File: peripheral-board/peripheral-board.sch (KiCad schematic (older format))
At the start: 4 parts, among them CON1001 AVR-ISP-10, IC1001 ATTINY48-A, P1001 Peripheral Bus, P1002 Power

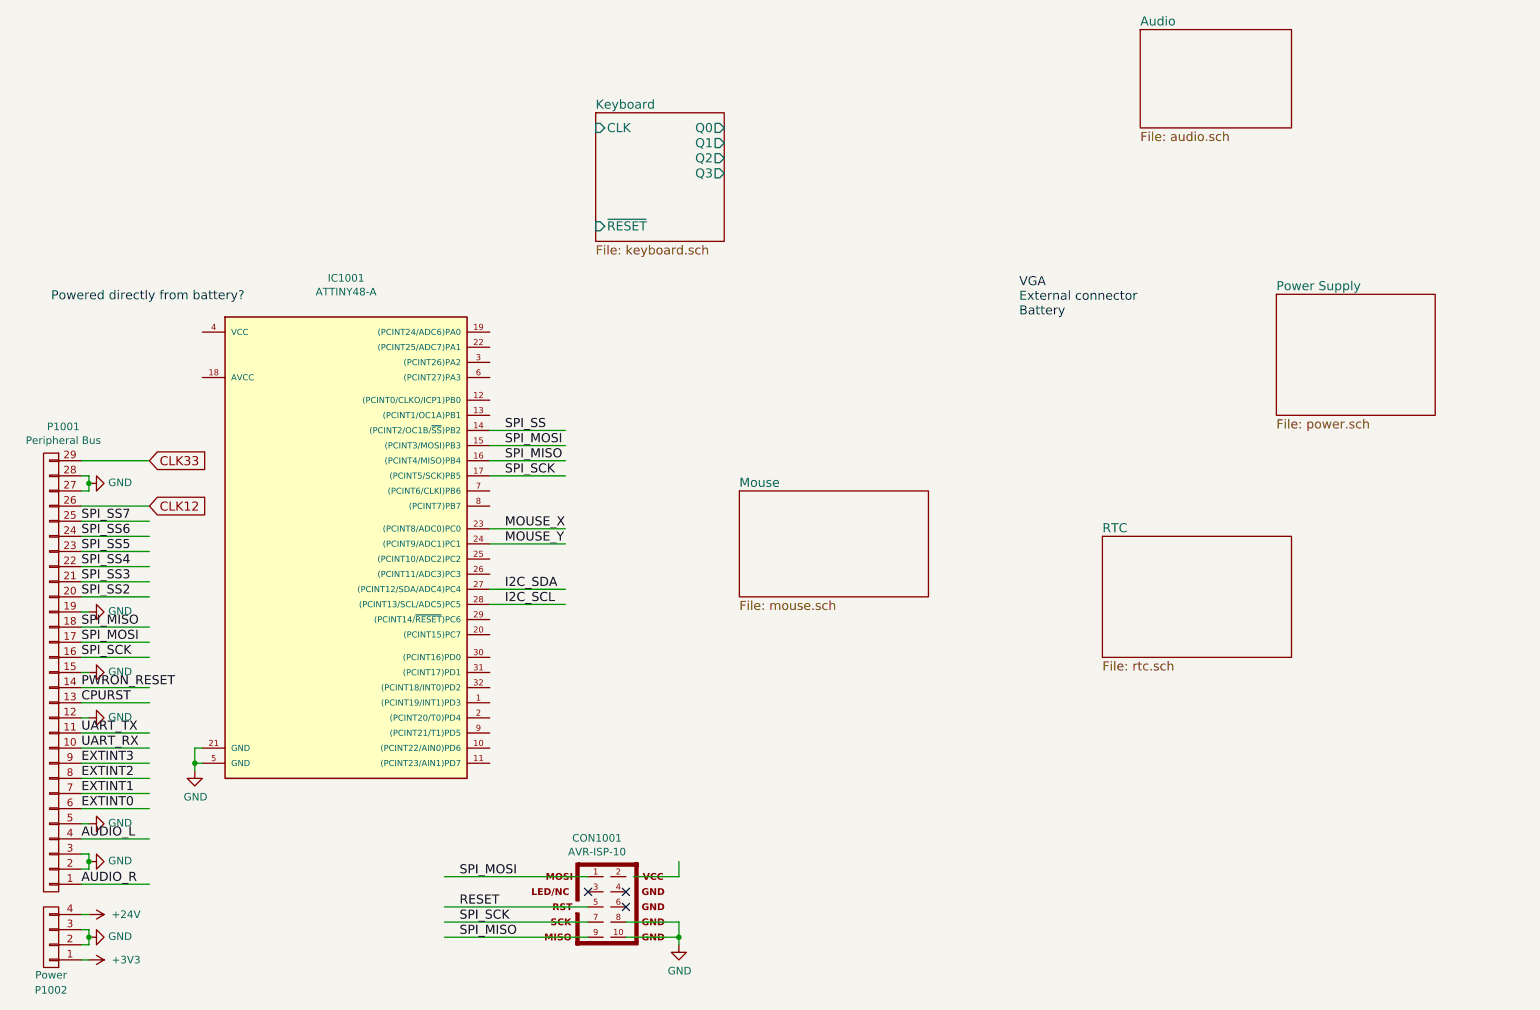
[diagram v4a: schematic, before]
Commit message: keyboard switches and diodes placed
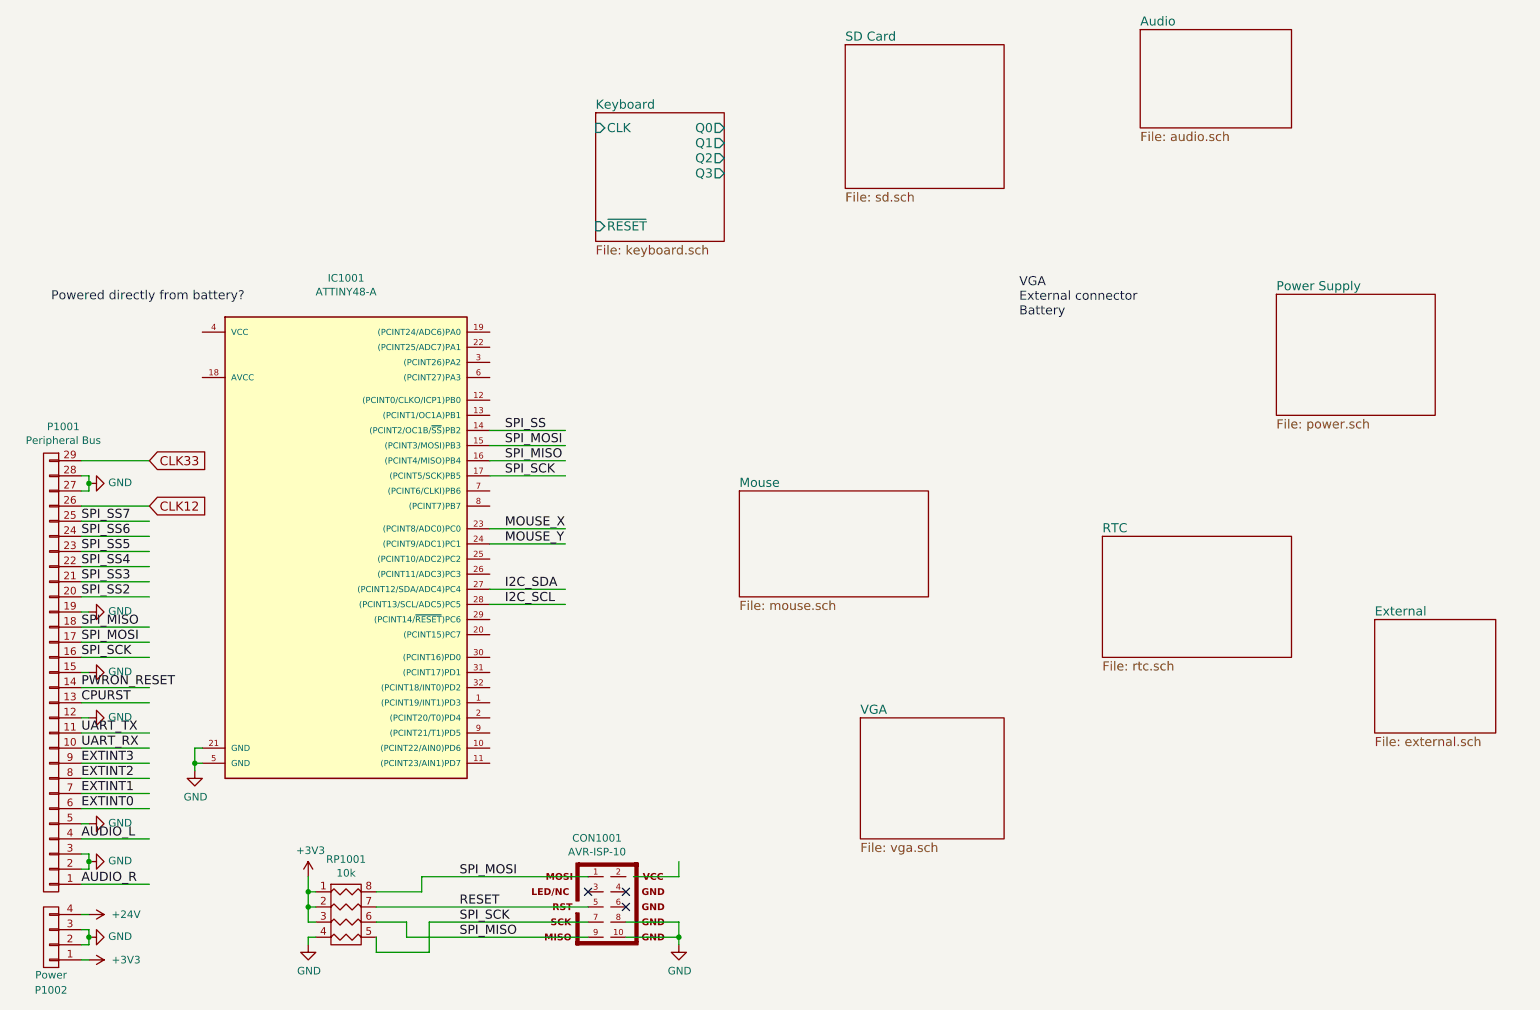
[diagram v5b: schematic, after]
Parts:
- added RP1001: 10k, Resistors_SMD:R_Cat16-4, symbol R_PACK4
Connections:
- wire segments 56 -> 69
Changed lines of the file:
@@
 LIBS:valves
 LIBS:amp
+LIBS:card-edge
 LIBS:peripheral-board-cache
 EELAYER 25 0
@@
 $Descr A4 11693 8268
 encoding utf-8
-Sheet 1 6
+Sheet 1 9
 Title ""
 Date ""
@@
 SPI_SCK
 $Comp
-L GND #PWR1010
+L GND #PWR1012
 U 1 1 581F4F29
 P 5150 6850
-F 0 "#PWR1010" H 5150 6600 50  0001 C CNN
+F 0 "#PWR1012" H 5150 6600 50  0001 C CNN
 F 1 "GND" H 5155 6677 50  0000 C CNN
 F 2 "" H 5150 6850 50  0000 C CNN
@@
 	-1   0    0    1
 $EndComp
-Wire Wire Line
-	3900 3450 4400 3450
-Wire Wire Line
-	3900 3550 4400 3550
-Wire Wire Line
-	3900 3650 4400 3650
-Wire Wire Line
-	3900 3750 4400 3750
-Wire Wire Line
-	3900 4500 4400 4500
-Wire Wire Line
-	3900 4600 4400 4600
-Wire Wire Line
-	3900 4100 4400 4100
-Wire Wire Line
-	3900 4200 4400 4200
-Wire Wire Line
-	4550 6400 3600 6400
-Wire Wire Line
-	4550 6600 3600 6600
-Wire Wire Line
-	4550 6700 3600 6700
-Wire Wire Line
-	4550 6800 3600 6800
-Wire Wire Line
-	4850 6400 5150 6400
-Wire Wire Line
-	5150 6400 5150 6300
-Wire Wire Line
-	4800 6700 5150 6700
-Wire Wire Line
-	5150 6700 5150 6850
-Wire Wire Line
-	4800 6800 5150 6800
-Connection ~ 5150 6800
-Wire Wire Line
-	2000 5550 1950 5550
-Wire Wire Line
-	1950 5550 1950 5700
-Wire Wire Line
-	2000 5650 1950 5650
-Connection ~ 1950 5650
-Wire Wire Line
-	1200 3950 1650 3950
-Wire Wire Line
-	1200 4050 1650 4050
-Wire Wire Line
-	1200 4150 1650 4150
-Wire Wire Line
-	1200 4250 1650 4250
-Wire Wire Line
-	1200 4350 1650 4350
-Wire Wire Line
-	1200 4450 1650 4450
-Wire Wire Line
-	1200 4550 1650 4550
-Wire Wire Line
-	1200 4750 1650 4750
-Wire Wire Line
-	1200 4850 1650 4850
-Wire Wire Line
-	1200 4950 1650 4950
-Wire Wire Line
-	1200 5150 1650 5150
-Wire Wire Line
-	1200 5250 1650 5250
-Wire Wire Line
-	1200 5450 1650 5450
-Wire Wire Line
-	1200 5550 1650 5550
-Wire Wire Line
-	1200 5650 1650 5650
-Wire Wire Line
-	1200 5750 1650 5750
-Wire Wire Line
-	1200 5850 1650 5850
-Wire Wire Line
-	1200 5950 1650 5950
-Wire Wire Line
-	1200 6150 1650 6150
-Wire Wire Line
-	1200 6450 1650 6450
 Text Label 1200 6450 0    60   ~ 0
 AUDIO_R
@@
 Text Label 1200 4050 0    60   ~ 0
 SPI_SS7
-Wire Wire Line
-	1200 3650 1650 3650
 Text GLabel 1650 3950 2    60   Input ~ 0
 CLK12
@@
 $EndComp
 $Comp
-L GND #PWR1009
+L GND #PWR1010
 U 1 1 581F7812
 P 1250 6800
-F 0 "#PWR1009" H 1250 6550 50  0001 C CNN
+F 0 "#PWR1010" H 1250 6550 50  0001 C CNN
 F 1 "GND" V 1255 6672 50  0000 R CNN
 F 2 "" H 1250 6800 50  0000 C CNN
@@
 	0    -1   -1   0
 $EndComp
-Wire Wire Line
-	1200 6750 1250 6750
-Wire Wire Line
-	1250 6750 1250 6850
-Wire Wire Line
-	1250 6850 1200 6850
-Connection ~ 1250 6800
-Wire Wire Line
-	1200 6250 1250 6250
-Wire Wire Line
-	1250 6250 1250 6350
-Wire Wire Line
-	1250 6350 1200 6350
-Connection ~ 1250 6300
-Wire Wire Line
-	1200 6050 1250 6050
-Wire Wire Line
-	1200 5350 1250 5350
-Wire Wire Line
-	1200 5050 1250 5050
-Wire Wire Line
-	1200 4650 1250 4650
-Wire Wire Line
-	1200 3750 1250 3750
-Wire Wire Line
-	1250 3750 1250 3850
-Wire Wire Line
-	1250 3850 1200 3850
-Connection ~ 1250 3800
-$Comp
-L +24V #PWR1008
+$Comp
+L +24V #PWR1009
 U 1 1 581F7F97
 P 1250 6650
-F 0 "#PWR1008" H 1250 6500 50  0001 C CNN
+F 0 "#PWR1009" H 1250 6500 50  0001 C CNN
 F 1 "+24V" V 1250 6800 50  0000 L CNN
 F 2 "" H 1250 6650 50  0000 C CNN
@@
 $EndComp
 $Comp
-L +3V3 #PWR1011
+L +3V3 #PWR1013
 U 1 1 581F7FED
 P 1250 6950
-F 0 "#PWR1011" H 1250 6800 50  0001 C CNN
+F 0 "#PWR1013" H 1250 6800 50  0001 C CNN
 F 1 "+3V3" V 1250 7100 50  0000 L CNN
 F 2 "" H 1250 6950 50  0000 C CNN
@@
 	0    1    1    0
 $EndComp
+$Sheet
+S 6250 900  1050 950
+U 581F67DF
+F0 "SD Card" 60
+F1 "sd.sch" 60
+$EndSheet
+$Comp
+L R_PACK4 RP1001
+U 1 1 581F7416
+P 2950 6850
+F 0 "RP1001" H 2950 7415 50  0000 C CNN
+F 1 "10k" H 2950 7324 50  0000 C CNN
+F 2 "Resistors_SMD:R_Cat16-4" H 2950 6850 50  0001 C CNN
+F 3 "" H 2950 6850 50  0000 C CNN
+	1    2950 6850
+	1    0    0    -1
+$EndComp
+Wire Wire Line
+	3900 3450 4400 3450
+Wire Wire Line
+	3900 3550 4400 3550
+Wire Wire Line
+	3900 3650 4400 3650
+Wire Wire Line
+	3900 3750 4400 3750
+Wire Wire Line
+	3900 4500 4400 4500
+Wire Wire Line
+	3900 4600 4400 4600
+Wire Wire Line
+	3900 4100 4400 4100
+Wire Wire Line
+	3900 4200 4400 4200
+Wire Wire Line
+	3450 6400 4550 6400
+Wire Wire Line
+	3150 6600 4550 6600
+Wire Wire Line
+	3500 6700 4550 6700
+Wire Wire Line
+	3350 6800 4550 6800
+Wire Wire Line
+	4850 6400 5150 6400
+Wire Wire Line
+	5150 6400 5150 6300
+Wire Wire Line
+	4800 6700 5150 6700
+Wire Wire Line
+	5150 6700 5150 6850
+Wire Wire Line
+	4800 6800 5150 6800
+Connection ~ 5150 6800
+Wire Wire Line
+	2000 5550 1950 5550
+Wire Wire Line
+	1950 5550 1950 5700
+Wire Wire Line
+	2000 5650 1950 5650
+Connection ~ 1950 5650
+Wire Wire Line
+	1200 3950 1650 3950
+Wire Wire Line
+	1200 4050 1650 4050
+Wire Wire Line
+	1200 4150 1650 4150
+Wire Wire Line
+	1200 4250 1650 4250
+Wire Wire Line
+	1200 4350 1650 4350
+Wire Wire Line
+	1200 4450 1650 4450
+Wire Wire Line
+	1200 4550 1650 4550
+Wire Wire Line
+	1200 4750 1650 4750
+Wire Wire Line
+	1200 4850 1650 4850
+Wire Wire Line
+	1200 4950 1650 4950
+Wire Wire Line
+	1200 5150 1650 5150
+Wire Wire Line
+	1200 5250 1650 5250
+Wire Wire Line
+	1200 5450 1650 5450
+Wire Wire Line
+	1200 5550 1650 5550
+Wire Wire Line
+	1200 5650 1650 5650
+Wire Wire Line
+	1200 5750 1650 5750
+Wire Wire Line
+	1200 5850 1650 5850
+Wire Wire Line
+	1200 5950 1650 5950
+Wire Wire Line
+	1200 6150 1650 6150
+Wire Wire Line
+	1200 6450 1650 6450
+Wire Wire Line
+	1200 3650 1650 3650
+Wire Wire Line
+	1200 6750 1250 6750
+Wire Wire Line
+	1250 6750 1250 6850
+Wire Wire Line
+	1250 6850 1200 6850
+Connection ~ 1250 6800
+Wire Wire Line
+	1200 6250 1250 6250
+Wire Wire Line
+	1250 6250 1250 6350
+Wire Wire Line
+	1250 6350 1200 6350
+Connection ~ 1250 6300
+Wire Wire Line
+	1200 6050 1250 6050
+Wire Wire Line
+	1200 5350 1250 5350
+Wire Wire Line
+	1200 5050 1250 5050
+Wire Wire Line
+	1200 4650 1250 4650
+Wire Wire Line
+	1200 3750 1250 3750
+Wire Wire Line
+	1250 3750 1250 3850
+Wire Wire Line
+	1250 3850 1200 3850
+Connection ~ 1250 3800
 Wire Wire Line
 	1250 6650 1200 6650
 Wire Wire Line
 	1250 6950 1200 6950
+Wire Wire Line
+	3450 6400 3450 6500
+Wire Wire Line
+	3450 6500 3150 6500
+Wire Wire Line
+	3350 6800 3350 6700
+Wire Wire Line
+	3350 6700 3150 6700
+Wire Wire Line
+	3500 6700 3500 6900
+Wire Wire Line
+	3500 6900 3150 6900
+Wire Wire Line
+	3150 6900 3150 6800
+$Comp
+L GND #PWR1011
+U 1 1 581F76DB
+P 2700 6850
+F 0 "#PWR1011" H 2700 6600 50  0001 C CNN
+F 1 "GND" H 2705 6677 50  0000 C CNN
+F 2 "" H 2700 6850 50  0000 C CNN
+F 3 "" H 2700 6850 50  0000 C CNN
+	1    2700 6850
+	1    0    0    -1
+$EndComp
+Wire Wire Line
+	2750 6800 2700 6800
+Wire Wire Line
+	2700 6800 2700 6850
+Wire Wire Line
+	2700 6700 2700 6400
+Wire Wire Line
+	2750 6600 2700 6600
+Connection ~ 2700 6600
+Wire Wire Line
+	2750 6700 2700 6700
+Wire Wire Line
+	2750 6500 2700 6500
+Connection ~ 2700 6500
+$Comp
+L +3V3 #PWR1008
+U 1 1 581F7984
+P 2700 6400
+F 0 "#PWR1008" H 2700 6250 50  0001 C CNN
+F 1 "+3V3" H 2715 6573 50  0000 C CNN
+F 2 "" H 2700 6400 50  0000 C CNN
+F 3 "" H 2700 6400 50  0000 C CNN
+	1    2700 6400
+	1    0    0    -1
+$EndComp
+$Sheet
+S 9750 4700 800  750
+U 581F7C47
+F0 "External" 60
+F1 "external.sch" 60
+$EndSheet
+$Sheet
+S 6350 5350 950  800
+U 581F8966
+F0 "VGA" 60
+F1 "vga.sch" 60
+$EndSheet
 $EndSCHEMATC

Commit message: lol
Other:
- note added: "Power button\nRGB led"
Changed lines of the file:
@@
 F1 "vga.sch" 60
 $EndSheet
+Text Notes 7400 2950 0    60   ~ 0
+Power button\nRGB led
 $EndSCHEMATC

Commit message: routed keyboard
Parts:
- added R1001, R1002: R, symbol R
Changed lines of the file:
@@
 LIBS:amp
 LIBS:card-edge
+LIBS:switchmode
+LIBS:joystick
 LIBS:peripheral-board-cache
 EELAYER 25 0
@@
 $EndSheet
 $Sheet
-S 5550 3850 1250 700
+S 6650 3100 1250 700
 U 5819E78C
 F0 "Mouse" 60
 F1 "mouse.sch" 60
+F2 "X" O R 7900 3200 60
+F3 "Y" O R 7900 3300 60
 $EndSheet
 $Comp
@@
 F0 "Power Supply" 60
 F1 "power.sch" 60
+F2 "~SHDN" I L 9100 2700 60
 $EndSheet
 $Sheet
@@
 F0 "RTC" 60
 F1 "rtc.sch" 60
+F2 "SCL" I L 7950 4250 60
+F3 "SDA" B L 7950 4350 60
 $EndSheet
 Text Notes 7400 2700 0    60   ~ 0
@@
 F0 "Audio" 60
 F1 "audio.sch" 60
+F2 "L" I L 8200 900 60
+F3 "R" I L 8200 1000 60
 $EndSheet
 $Comp
@@
 SPI_SCK
 $Comp
-L GND #PWR1012
+L GND #PWR01
 U 1 1 581F4F29
 P 5150 6850
-F 0 "#PWR1012" H 5150 6600 50  0001 C CNN
+F 0 "#PWR01" H 5150 6600 50  0001 C CNN
 F 1 "GND" H 5155 6677 50  0000 C CNN
 F 2 "" H 5150 6850 50  0000 C CNN
@@
 NoConn ~ 4550 6500
 $Comp
-L GND #PWR1005
+L GND #PWR02
 U 1 1 581F524B
 P 1950 5700
-F 0 "#PWR1005" H 1950 5450 50  0001 C CNN
+F 0 "#PWR02" H 1950 5450 50  0001 C CNN
 F 1 "GND" H 1955 5527 50  0000 C CNN
 F 2 "" H 1950 5700 50  0000 C CNN
@@
 CLK33
 $Comp
-L GND #PWR1001
+L GND #PWR03
 U 1 1 581F752E
 P 1250 3800
-F 0 "#PWR1001" H 1250 3550 50  0001 C CNN
+F 0 "#PWR03" H 1250 3550 50  0001 C CNN
 F 1 "GND" V 1255 3672 50  0000 R CNN
 F 2 "" H 1250 3800 50  0000 C CNN
@@
 $EndComp
 $Comp
-L GND #PWR1002
+L GND #PWR04
 U 1 1 581F7634
 P 1250 4650
-F 0 "#PWR1002" H 1250 4400 50  0001 C CNN
+F 0 "#PWR04" H 1250 4400 50  0001 C CNN
 F 1 "GND" V 1255 4522 50  0000 R CNN
 F 2 "" H 1250 4650 50  0000 C CNN
@@
 $EndComp
 $Comp
-L GND #PWR1003
+L GND #PWR05
 U 1 1 581F76B8
 P 1250 5050
-F 0 "#PWR1003" H 1250 4800 50  0001 C CNN
+F 0 "#PWR05" H 1250 4800 50  0001 C CNN
 F 1 "GND" V 1255 4922 50  0000 R CNN
 F 2 "" H 1250 5050 50  0000 C CNN
@@
 $EndComp
 $Comp
-L GND #PWR1004
+L GND #PWR06
 U 1 1 581F7709
 P 1250 5350
-F 0 "#PWR1004" H 1250 5100 50  0001 C CNN
+F 0 "#PWR06" H 1250 5100 50  0001 C CNN
 F 1 "GND" V 1255 5222 50  0000 R CNN
 F 2 "" H 1250 5350 50  0000 C CNN
@@
 $EndComp
 $Comp
-L GND #PWR1006
+L GND #PWR07
 U 1 1 581F7744
 P 1250 6050
-F 0 "#PWR1006" H 1250 5800 50  0001 C CNN
+F 0 "#PWR07" H 1250 5800 50  0001 C CNN
 F 1 "GND" V 1255 5922 50  0000 R CNN
 F 2 "" H 1250 6050 50  0000 C CNN
@@
 $EndComp
 $Comp
-L GND #PWR1007
+L GND #PWR08
 U 1 1 581F77D7
 P 1250 6300
-F 0 "#PWR1007" H 1250 6050 50  0001 C CNN
+F 0 "#PWR08" H 1250 6050 50  0001 C CNN
 F 1 "GND" V 1255 6172 50  0000 R CNN
 F 2 "" H 1250 6300 50  0000 C CNN
@@
 $EndComp
 $Comp
-L GND #PWR1010
+L GND #PWR09
 U 1 1 581F7812
 P 1250 6800
-F 0 "#PWR1010" H 1250 6550 50  0001 C CNN
+F 0 "#PWR09" H 1250 6550 50  0001 C CNN
 F 1 "GND" V 1255 6672 50  0000 R CNN
 F 2 "" H 1250 6800 50  0000 C CNN
@@
 $EndComp
 $Comp
-L +24V #PWR1009
+L +24V #PWR010
 U 1 1 581F7F97
 P 1250 6650
-F 0 "#PWR1009" H 1250 6500 50  0001 C CNN
+F 0 "#PWR010" H 1250 6500 50  0001 C CNN
 F 1 "+24V" V 1250 6800 50  0000 L CNN
 F 2 "" H 1250 6650 50  0000 C CNN
@@
 $EndComp
 $Comp
-L +3V3 #PWR1013
+L +3V3 #PWR011
 U 1 1 581F7FED
 P 1250 6950
-F 0 "#PWR1013" H 1250 6800 50  0001 C CNN
+F 0 "#PWR011" H 1250 6800 50  0001 C CNN
 F 1 "+3V3" V 1250 7100 50  0000 L CNN
 F 2 "" H 1250 6950 50  0000 C CNN
@@
 F0 "SD Card" 60
 F1 "sd.sch" 60
+F2 "MISO" O L 6250 1000 60
+F3 "MOSI" I L 6250 1100 60
+F4 "SS" I L 6250 1200 60
+F5 "SCK" I L 6250 1300 60
+F6 "WP" O R 7300 1000 60
+F7 "DETECT" O R 7300 1100 60
 $EndSheet
 $Comp
@@
 	3150 6900 3150 6800
 $Comp
-L GND #PWR1011
+L GND #PWR012
 U 1 1 581F76DB
 P 2700 6850
-F 0 "#PWR1011" H 2700 6600 50  0001 C CNN
+F 0 "#PWR012" H 2700 6600 50  0001 C CNN
 F 1 "GND" H 2705 6677 50  0000 C CNN
 F 2 "" H 2700 6850 50  0000 C CNN
@@
 Connection ~ 2700 6500
 $Comp
-L +3V3 #PWR1008
+L +3V3 #PWR013
 U 1 1 581F7984
 P 2700 6400
-F 0 "#PWR1008" H 2700 6250 50  0001 C CNN
+F 0 "#PWR013" H 2700 6250 50  0001 C CNN
 F 1 "+3V3" H 2715 6573 50  0000 C CNN
 F 2 "" H 2700 6400 50  0000 C CNN
@@
 Text Notes 7400 2950 0    60   ~ 0
 Power button\nRGB led
+$Comp
+L R R1001
+U 1 1 58224307
+P 4650 4500
+F 0 "R1001" V 4550 4500 50  0000 C CNN
+F 1 "R" V 4650 4500 50  0000 C CNN
+F 2 "" V 4580 4500 50  0000 C CNN
+F 3 "" H 4650 4500 50  0000 C CNN
+	1    4650 4500
+	0    1    1    0
+$EndComp
+$Comp
+L R R1002
+U 1 1 582244B8
+P 4650 4600
+F 0 "R1002" V 4750 4600 50  0000 C CNN
+F 1 "R" V 4650 4600 50  0000 C CNN
+F 2 "" V 4580 4600 50  0000 C CNN
+F 3 "" H 4650 4600 50  0000 C CNN
+	1    4650 4600
+	0    1    1    0
+$EndComp
 $EndSCHEMATC
